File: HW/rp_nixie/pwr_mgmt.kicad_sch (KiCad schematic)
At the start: 1 part

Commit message: updated gitignore
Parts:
- added U1: MC33063AD, Package_SO:SOIC-8_3.9x4.9mm_P1.27mm, symbol Regulator_Switching:MC33063AD
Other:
- note removed: "LM51561H"
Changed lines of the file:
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@@
 (kicad_sch (version 20230121) (generator eeschema)
   (paper "A4")
-  (text "LM51561H" (at 126.365 89.535 0)
-    (effects (font (size 1.27 1.27)) (justify left bottom))
-  )
   (text "5V input\n3v3 out\ngenerate 20-200V\n(variable HV supply)\nfiltering, bulk bypass"
     (at 214.63 179.07 0)
@@
         )
       )
+    )
+  )
+  (symbol (lib_id "Regulator_Switching:MC33063AD") (at 122.555 91.44 0) (unit 1)
+    (in_bom yes) (on_board yes) (dnp no) (fields_autoplaced)
+    (property "Reference" "U1" (at 122.555 79.375 0)
+      (effects (font (size 1.27 1.27)))
+    )
+    (property "Value" "MC33063AD" (at 122.555 81.915 0)
+      (effects (font (size 1.27 1.27)))
+    )
+    (property "Footprint" "Package_SO:SOIC-8_3.9x4.9mm_P1.27mm" (at 123.825 102.87 0)
+      (effects (font (size 1.27 1.27)) (justify left) hide)
+    )
+    (property "Datasheet" "http://www.onsemi.com/pub_link/Collateral/MC34063A-D.PDF" (at 135.255 93.98 0)
+      (effects (font (size 1.27 1.27)) hide)
+    )
+    (pin "1")
+    (pin "2")
+    (pin "3")
+    (pin "4")
+    (pin "5")
+    (pin "6")
+    (pin "7")
+    (pin "8")
+    (instances
+      (project "rp_nixie"
+        (path "/56c65019-066c-47cb-99e5-7a3ed779dcda/f8c880ea-79c5-432f-81fa-d32cf5a8db8f"
+          (reference "U1") (unit 1)
+        )
+      )

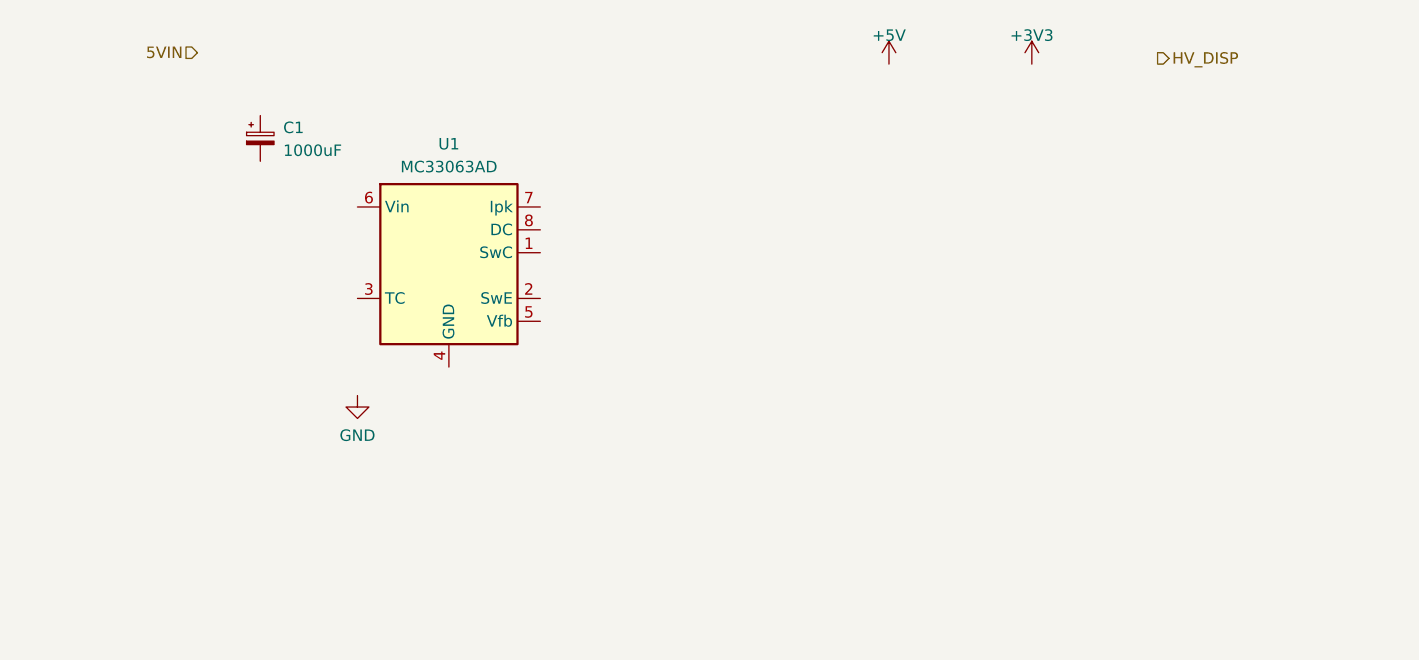
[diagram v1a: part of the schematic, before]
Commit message: added better boost circuit
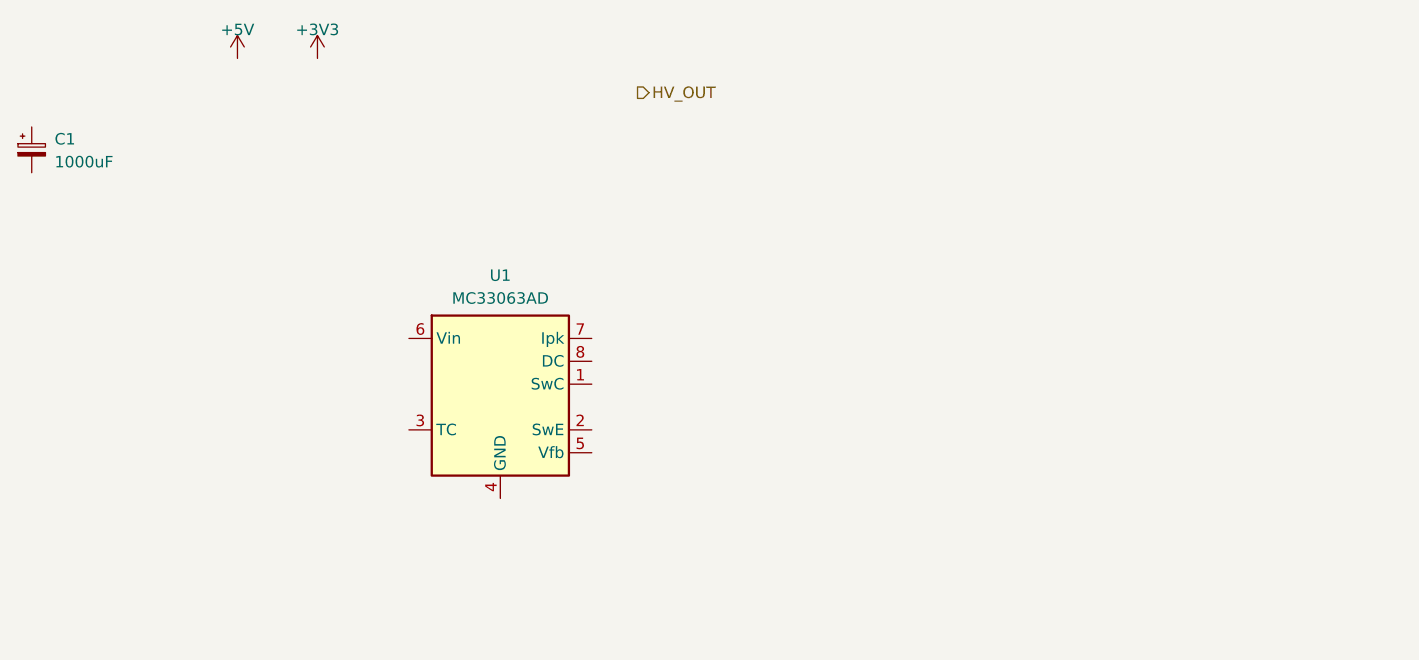
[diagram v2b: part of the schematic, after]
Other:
- moved on the sheet: C1
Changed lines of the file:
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@@
     (effects (font (size 1.27 1.27)) (justify left bottom))
   )
-  (hierarchical_label "5VIN" (shape input) (at 94.615 69.215 180) (fields_autoplaced)
-    (effects (font (size 1.27 1.27)) (justify right))
-  )
-  (hierarchical_label "HV_DISP" (shape output) (at 201.295 69.85 0) (fields_autoplaced)
+  (hierarchical_label "HV_OUT" (shape output) (at 143.51 73.66 0) (fields_autoplaced)
     (effects (font (size 1.27 1.27)) (justify left))
   )
-  (symbol (lib_id "power:+3V3") (at 187.325 70.485 0) (unit 1)
+  (symbol (lib_id "power:+3V3") (at 107.95 69.85 0) (unit 1)
     (in_bom yes) (on_board yes) (dnp no) (fields_autoplaced)
-    (property "Reference" "#PWR02" (at 187.325 74.295 0)
+    (property "Reference" "#PWR02" (at 107.95 73.66 0)
       (effects (font (size 1.27 1.27)) hide)
     )
-    (property "Value" "+3V3" (at 187.325 67.31 0)
+    (property "Value" "+3V3" (at 107.95 66.675 0)
       (effects (font (size 1.27 1.27)))
     )
-    (property "Footprint" "" (at 187.325 70.485 0)
+    (property "Footprint" "" (at 107.95 69.85 0)
       (effects (font (size 1.27 1.27)) hide)
     )
-    (property "Datasheet" "" (at 187.325 70.485 0)
+    (property "Datasheet" "" (at 107.95 69.85 0)
       (effects (font (size 1.27 1.27)) hide)
     )
@@
     )
   )
-  (symbol (lib_id "power:+5V") (at 171.45 70.485 0) (unit 1)
+  (symbol (lib_id "power:+5V") (at 99.06 69.85 0) (unit 1)
     (in_bom yes) (on_board yes) (dnp no) (fields_autoplaced)
-    (property "Reference" "#PWR01" (at 171.45 74.295 0)
+    (property "Reference" "#PWR01" (at 99.06 73.66 0)
       (effects (font (size 1.27 1.27)) hide)
     )
-    (property "Value" "+5V" (at 171.45 67.31 0)
+    (property "Value" "+5V" (at 99.06 66.675 0)
       (effects (font (size 1.27 1.27)))
     )
-    (property "Footprint" "" (at 171.45 70.485 0)
+    (property "Footprint" "" (at 99.06 69.85 0)
       (effects (font (size 1.27 1.27)) hide)
     )
-    (property "Datasheet" "" (at 171.45 70.485 0)
+    (property "Datasheet" "" (at 99.06 69.85 0)
       (effects (font (size 1.27 1.27)) hide)
     )
@@
     )
   )
-  (symbol (lib_id "Device:C_Polarized_Small") (at 101.6 78.74 0) (unit 1)
+  (symbol (lib_id "Device:C_Polarized_Small") (at 76.2 80.01 0) (unit 1)
     (in_bom yes) (on_board yes) (dnp no) (fields_autoplaced)
-    (property "Reference" "C1" (at 104.14 77.5589 0)
+    (property "Reference" "C1" (at 78.74 78.8289 0)
       (effects (font (size 1.27 1.27)) (justify left))
     )
-    (property "Value" "1000uF" (at 104.14 80.0989 0)
+    (property "Value" "1000uF" (at 78.74 81.3689 0)
       (effects (font (size 1.27 1.27)) (justify left))
     )
-    (property "Footprint" "Capacitor_SMD:CP_Elec_10x10" (at 101.6 78.74 0)
+    (property "Footprint" "Capacitor_SMD:CP_Elec_10x10" (at 76.2 80.01 0)
       (effects (font (size 1.27 1.27)) hide)
     )
-    (property "Datasheet" "https://datasheet.lcsc.com/lcsc/1811051743_Lelon-VE-102M1CTR-1010_C249474.pdf" (at 101.6 78.74 0)
+    (property "Datasheet" "https://datasheet.lcsc.com/lcsc/1811051743_Lelon-VE-102M1CTR-1010_C249474.pdf" (at 76.2 80.01 0)
       (effects (font (size 1.27 1.27)) hide)
     )
-    (property "PN" "VE-102M1CTR-1010" (at 101.6 78.74 0)
+    (property "PN" "VE-102M1CTR-1010" (at 76.2 80.01 0)
       (effects (font (size 1.27 1.27)) hide)
     )
@@
     )
   )
-  (symbol (lib_id "power:GND") (at 112.395 107.315 0) (unit 1)
+  (symbol (lib_id "Regulator_Switching:MC33063AD") (at 128.27 106.045 0) (unit 1)
     (in_bom yes) (on_board yes) (dnp no) (fields_autoplaced)
-    (property "Reference" "#PWR03" (at 112.395 113.665 0)
+    (property "Reference" "U1" (at 128.27 93.98 0)
+      (effects (font (size 1.27 1.27)))
+    )
+    (property "Value" "MC33063AD" (at 128.27 96.52 0)
+      (effects (font (size 1.27 1.27)))
+    )
+    (property "Footprint" "Package_SO:SOIC-8_3.9x4.9mm_P1.27mm" (at 129.54 117.475 0)
+      (effects (font (size 1.27 1.27)) (justify left) hide)
+    )
+    (property "Datasheet" "http://www.onsemi.com/pub_link/Collateral/MC34063A-D.PDF" (at 140.97 108.585 0)
       (effects (font (size 1.27 1.27)) hide)
     )
-    (property "Value" "GND" (at 112.395 111.76 0)
-      (effects (font (size 1.27 1.27)))
-    )
-    (property "Footprint" "" (at 112.395 107.315 0)
-      (effects (font (size 1.27 1.27)) hide)
-    )
-    (property "Datasheet" "" (at 112.395 107.315 0)
-      (effects (font (size 1.27 1.27)) hide)
-    )
-    (pin "1")
-    (instances
-      (project "rp_nixie"
-        (path "/56c65019-066c-47cb-99e5-7a3ed779dcda/f8c880ea-79c5-432f-81fa-d32cf5a8db8f"
-          (reference "#PWR03") (unit 1)
-        )
-      )
-    )
-  )
-  (symbol (lib_id "Regulator_Switching:MC33063AD") (at 122.555 91.44 0) (unit 1)
-    (in_bom yes) (on_board yes) (dnp no) (fields_autoplaced)
-    (property "Reference" "U1" (at 122.555 79.375 0)
-      (effects (font (size 1.27 1.27)))
-    )
-    (property "Value" "MC33063AD" (at 122.555 81.915 0)
-      (effects (font (size 1.27 1.27)))
-    )
-    (property "Footprint" "Package_SO:SOIC-8_3.9x4.9mm_P1.27mm" (at 123.825 102.87 0)
-      (effects (font (size 1.27 1.27)) (justify left) hide)
-    )
-    (property "Datasheet" "http://www.onsemi.com/pub_link/Collateral/MC34063A-D.PDF" (at 135.255 93.98 0)
-      (effects (font (size 1.27 1.27)) hide)
-    )

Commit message: finished MCU and IO
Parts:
- removed U1: MC33063AD, Package_SO:SOIC-8_3.9x4.9mm_P1.27mm, symbol Regulator_Switching:MC33063AD
- added C2: 100nF, symbol Device:C_Small
- added C3: 2.2nF, symbol Device:C_Small
- added C4: 4.7uF, Capacitor_SMD:CP_Elec_10x10, symbol Device:C_Polarized_Small
- added D1: RS1M, symbol Device:D
- added L1: 220u, symbol Device:L_Small
- added Q1: FZT857TA, symbol Simulation_SPICE:NPN
- added R1: 0.7, symbol Device:R_Small
- added R2: 180, symbol Device:R_Small
- added R3: 10k, symbol Device:R_Small
- added R4: 470, symbol Device:R_Small
- added R5: 200k, symbol Device:R_Small
- added R6: 1k, symbol Device:R_Small
- added RV1: 100k, symbol Device:R_Potentiometer
- added U2: MC33063AD, Package_SO:SOIC-8_3.9x4.9mm_P1.27mm, symbol Regulator_Switching:MC33063AD
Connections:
- net +5V: now also C1.1, C2.1, R1.2, R4.1, U2.6 (Vin)
- net HV_OUT: now also C4.1, D1.1 (K), R5.2
- net GND: now reaches C1.2
- net GND: now also C2.2, C3.2, C4.2, Q1.3 (E), R3.2, R6.2, U2.4 (GND)
- new net: L1.1, R1.1, R2.2, U2.7 (Ipk)
- new net: D1.2 (A), L1.2, Q1.1 (C)
- new net: R5.1, RV1.1
- new net DC: R2.1, U2.8 (DC)
- new net SwC: R4.2, U2.1 (SwC)
- new net SwE: Q1.2 (B), R3.1, U2.2 (SwE)
- new net TC: C3.1, U2.3 (TC)
- new net Vfb: R6.1, RV1.2, RV1.3, U2.5 (Vfb)
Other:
- note added: "HV Supply"
- moved on the sheet: C1

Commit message: some schematic work
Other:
- moved on the sheet: C1, C2, C3, C4, D1, L1, Q1, R1, R2, R3, R4, R5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
